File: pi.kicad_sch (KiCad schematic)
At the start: 12 parts, among them CN2 539160208

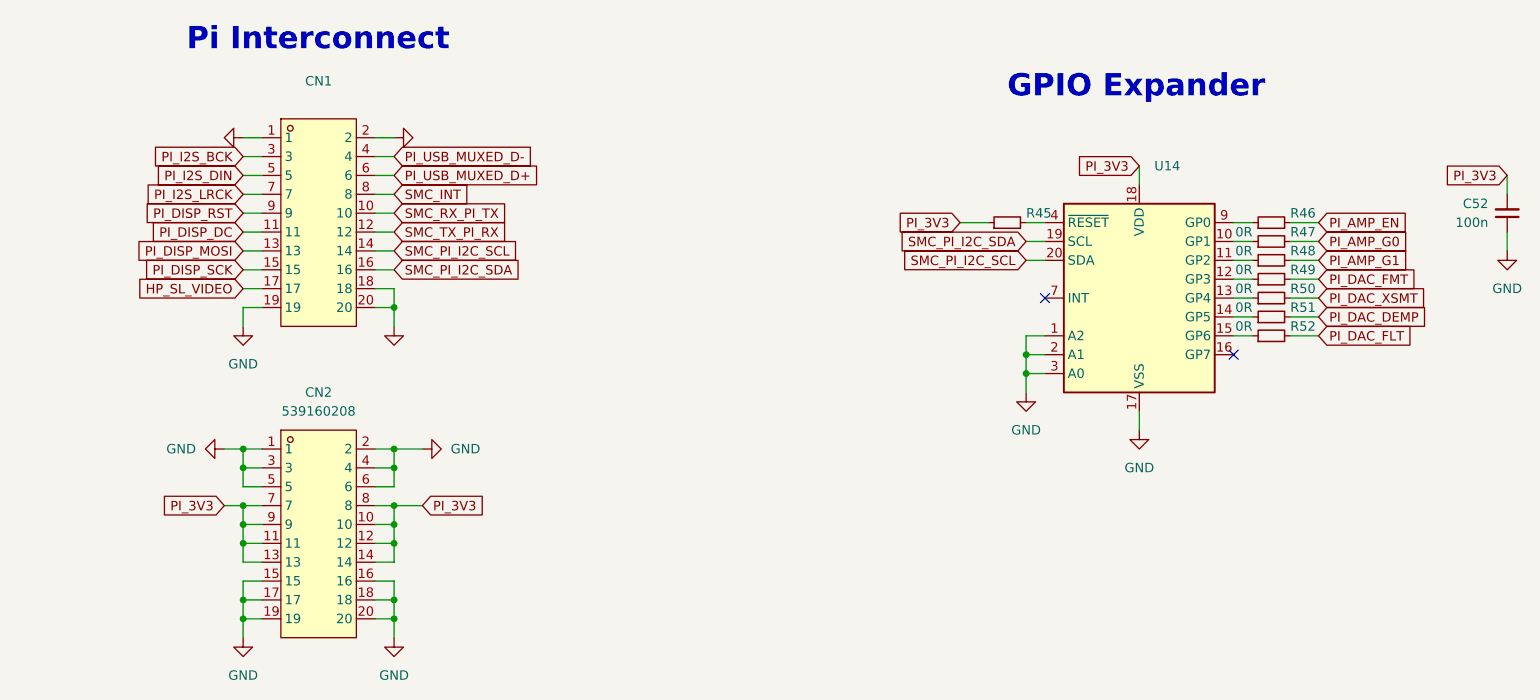
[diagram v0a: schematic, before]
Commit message: analysis: specify pi will be powered directly from VCC
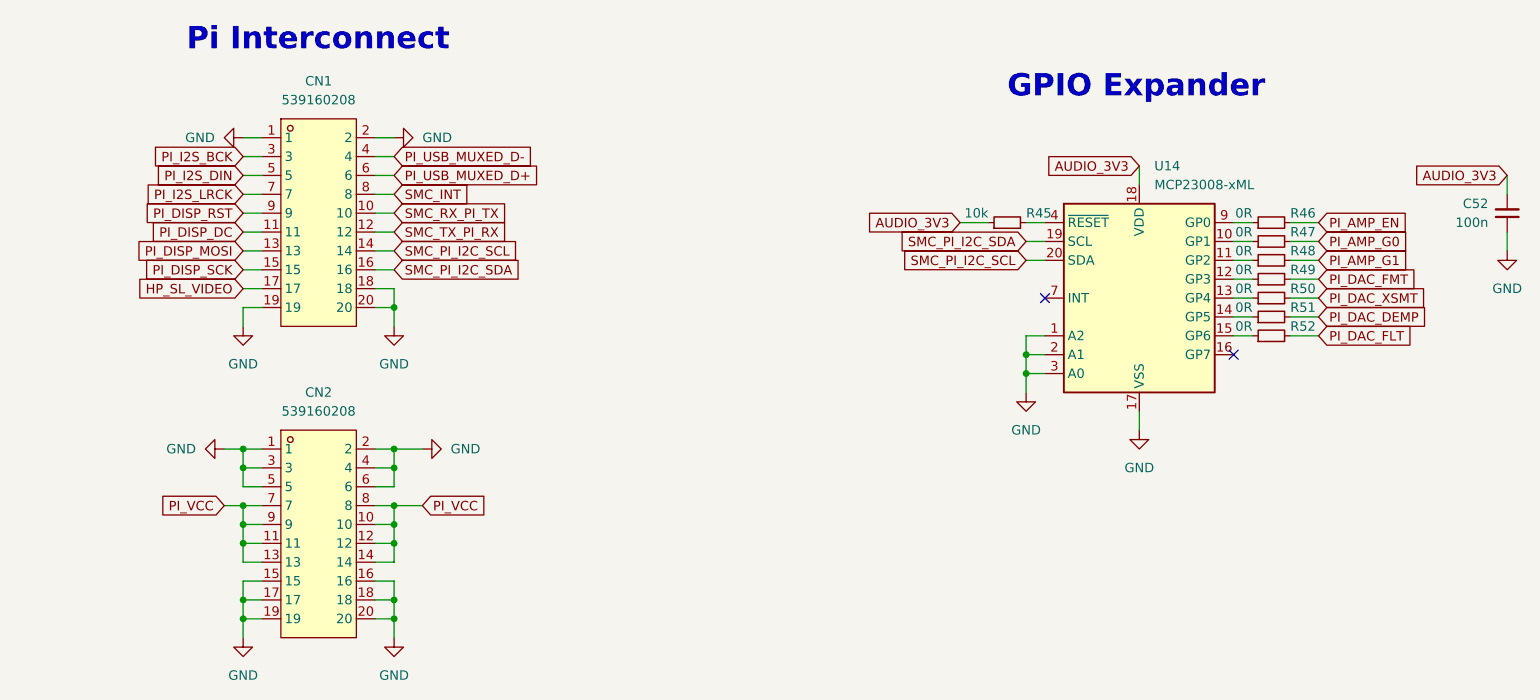
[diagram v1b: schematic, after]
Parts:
- C52: footprint (none) -> Capacitor_SMD:C_0402_1005Metric
- CN1: value (none) -> 539160208
- R45: value (none) -> 10k; footprint (none) -> Resistor_SMD:R_0402_1005Metric
- R46: value (none) -> 0R; footprint (none) -> Resistor_SMD:R_0402_1005Metric
- R47, R48, R49, R50, R51, R52: footprint (none) -> Resistor_SMD:R_0402_1005Metric
- U14: value (none) -> MCP23008-xML
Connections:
- net PI_3V3 renamed PI_VCC
- net PI_VCC: no longer C52.2, R45.1, U14.18 (VDD)
- new net AUDIO_3V3: C52.2, R45.1, U14.18 (VDD)
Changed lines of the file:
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@@
     (effects (font (size 3 3) (thickness 0.6) bold) (justify left bottom))
   )
+  (global_label "AUDIO_3V3" (shape input) (at 168.91 69.85 180) (fields_autoplaced)
+    (effects (font (size 1.27 1.27)) (justify right))
+    (property "Intersheet References" "${INTERSHEET_REFS}" (id 0) (at 156.3974 69.9294 0)
+      (effects (font (size 1.27 1.27)) (justify right) hide)
+    )
+  )
   (global_label "PI_AMP_G1" (shape input) (at 193.04 82.55 0) (fields_autoplaced)
     (effects (font (size 1.27 1.27)) (justify left))
@@
     )
   )
-  (global_label "PI_3V3" (shape input) (at 168.91 69.85 180) (fields_autoplaced)
-    (effects (font (size 1.27 1.27)) (justify right))
-    (property "Intersheet References" "${INTERSHEET_REFS}" (id 0) (at 160.1469 69.9294 0)
-      (effects (font (size 1.27 1.27)) (justify right) hide)
-    )
-  )
   (global_label "SMC_PI_I2C_SCL" (shape input) (at 153.67 82.55 180) (fields_autoplaced)
     (effects (font (size 1.27 1.27)) (justify right))
@@
     )
   )
-  (global_label "PI_3V3" (shape input) (at 144.78 77.47 180) (fields_autoplaced)
-    (effects (font (size 1.27 1.27)) (justify right))
-    (property "Intersheet References" "${INTERSHEET_REFS}" (id 0) (at 136.0169 77.5494 0)
-      (effects (font (size 1.27 1.27)) (justify right) hide)
-    )
-  )
   (global_label "PI_I2S_BCK" (shape input) (at 48.26 68.58 180) (fields_autoplaced)
     (effects (font (size 1.27 1.27)) (justify right))
@@
     )
   )
-  (global_label "PI_3V3" (shape input) (at 45.72 115.57 180) (fields_autoplaced)
+  (global_label "AUDIO_3V3" (shape input) (at 144.78 77.47 180) (fields_autoplaced)
+    (effects (font (size 1.27 1.27)) (justify right))
+    (property "Intersheet References" "${INTERSHEET_REFS}" (id 0) (at 132.2674 77.5494 0)
+      (effects (font (size 1.27 1.27)) (justify right) hide)
+    )
+  )
+  (global_label "PI_VCC" (shape input) (at 45.72 115.57 180) (fields_autoplaced)
     (effects (font (size 1.27 1.27)) (justify right))
     (property "Intersheet References" "${INTERSHEET_REFS}" (id 0) (at 36.9569 115.6494 0)
@@
     )
   )
-  (global_label "PI_3V3" (shape input) (at 72.39 115.57 0) (fields_autoplaced)
+  (global_label "PI_VCC" (shape input) (at 72.39 115.57 0) (fields_autoplaced)
     (effects (font (size 1.27 1.27)) (justify left))
     (property "Intersheet References" "${INTERSHEET_REFS}" (id 0) (at 81.1531 115.4906 0)
@@
     )
   )
-  (global_label "PI_3V3" (shape input) (at 218.44 71.12 180) (fields_autoplaced)
-    (effects (font (size 1.27 1.27)) (justify right))
-    (property "Intersheet References" "${INTERSHEET_REFS}" (id 0) (at 209.6769 71.1994 0)
+  (global_label "AUDIO_3V3" (shape input) (at 218.44 71.12 180) (fields_autoplaced)
+    (effects (font (size 1.27 1.27)) (justify right))
+    (property "Intersheet References" "${INTERSHEET_REFS}" (id 0) (at 205.9274 71.1994 0)
       (effects (font (size 1.27 1.27)) (justify right) hide)
     )
@@
       (effects (font (size 1.27 1.27)) (justify right))
     )
-    (property "Value" "" (id 1) (at 184.15 76.2 90)
-      (effects (font (size 1.27 1.27)) (justify left))
-    )
-    (property "Footprint" "" (id 2) (at 186.69 77.47 0)
+    (property "Value" "0R" (id 1) (at 184.15 76.2 90)
+      (effects (font (size 1.27 1.27)) (justify left))
+    )
+    (property "Footprint" "Resistor_SMD:R_0402_1005Metric" (id 2) (at 186.69 77.47 0)
       (effects (font (size 1.27 1.27)) hide)
     )
@@
       (effects (font (size 1.27 1.27)) (justify right))
     )
-    (property "Value" "" (id 1) (at 148.59 76.2 90)
-      (effects (font (size 1.27 1.27)) (justify left))
-    )
-    (property "Footprint" "" (id 2) (at 151.13 77.47 0)
+    (property "Value" "10k" (id 1) (at 148.59 76.2 90)
+      (effects (font (size 1.27 1.27)) (justify left))
+    )
+    (property "Footprint" "Resistor_SMD:R_0402_1005Metric" (id 2) (at 151.13 77.47 0)
       (effects (font (size 1.27 1.27)) hide)
     )
@@
       (effects (font (size 1.27 1.27)) (justify left))
     )
-    (property "Footprint" "" (id 2) (at 186.69 87.63 0)
+    (property "Footprint" "Resistor_SMD:R_0402_1005Metric" (id 2) (at 186.69 87.63 0)
       (effects (font (size 1.27 1.27)) hide)
     )
@@
       (effects (font (size 1.27 1.27)) (justify left))
     )
-    (property "Value" "" (id 1) (at 170.9294 72.39 0)
+    (property "Value" "MCP23008-xML" (id 1) (at 170.9294 72.39 0)
       (effects (font (size 1.27 1.27)) (justify left))
     )
@@
       (effects (font (size 1.27 1.27)) hide)
     )
-    (property "Value" "" (id 1) (at 68.58 96.52 0))
+    (property "Value" "GND" (id 1) (at 68.58 96.52 0))
     (property "Footprint" "" (id 2) (at 68.58 91.44 0)
       (effects (font (size 1.27 1.27)) hide)
@@
       (effects (font (size 1.27 1.27)) (justify left))
     )
-    (property "Footprint" "" (id 2) (at 186.69 92.71 0)
+    (property "Footprint" "Resistor_SMD:R_0402_1005Metric" (id 2) (at 186.69 92.71 0)
       (effects (font (size 1.27 1.27)) hide)
     )
@@
       (effects (font (size 1.27 1.27)) (justify left))
     )
-    (property "Footprint" "" (id 2) (at 186.69 85.09 0)
+    (property "Footprint" "Resistor_SMD:R_0402_1005Metric" (id 2) (at 186.69 85.09 0)
       (effects (font (size 1.27 1.27)) hide)
     )
@@
       (effects (font (size 1.27 1.27)) hide)
     )
-    (property "Value" "" (id 1) (at 72.39 66.0399 90)
+    (property "Value" "GND" (id 1) (at 72.39 66.0399 90)
       (effects (font (size 1.27 1.27)) (justify right))
     )
@@
       (effects (font (size 1.27 1.27)) (justify right))
     )
-    (property "Footprint" "" (id 2) (at 218.44 76.2 0)
+    (property "Footprint" "Capacitor_SMD:C_0402_1005Metric" (id 2) (at 218.44 76.2 0)
       (effects (font (size 1.27 1.27)) hide)
     )
@@
       (effects (font (size 1.27 1.27)) (justify left))
     )
-    (property "Footprint" "" (id 2) (at 186.69 90.17 0)
+    (property "Footprint" "Resistor_SMD:R_0402_1005Metric" (id 2) (at 186.69 90.17 0)
       (effects (font (size 1.27 1.27)) hide)
     )
@@
       (effects (font (size 1.27 1.27)) (justify left))
     )
-    (property "Footprint" "" (id 2) (at 186.69 80.01 0)
+    (property "Footprint" "Resistor_SMD:R_0402_1005Metric" (id 2) (at 186.69 80.01 0)
       (effects (font (size 1.27 1.27)) hide)
     )
@@
       (effects (font (size 1.27 1.27)) (justify left))
     )
-    (property "Footprint" "" (id 2) (at 186.69 82.55 0)
+    (property "Footprint" "Resistor_SMD:R_0402_1005Metric" (id 2) (at 186.69 82.55 0)
       (effects (font (size 1.27 1.27)) hide)
     )
@@
       (effects (font (size 1.27 1.27)) hide)
     )
-    (property "Value" "" (id 1) (at 44.45 66.0399 90)
+    (property "Value" "GND" (id 1) (at 44.45 66.0399 90)
       (effects (font (size 1.27 1.27)) (justify right))
     )
@@
     (in_bom yes) (on_board yes) (fields_autoplaced)
     (property "Reference" "CN1" (id 0) (at 58.42 58.42 0))
-    (property "Value" "" (id 1) (at 58.42 60.96 0))
+    (property "Value" "539160208" (id 1) (at 58.42 60.96 0))
     (property "Footprint" "lcsc:CONN-SMD_539160208" (id 2) (at 58.42 96.52 0)
       (effects (font (size 1.27 1.27)) hide)

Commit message: integration: add mounting holes and connectors and second board
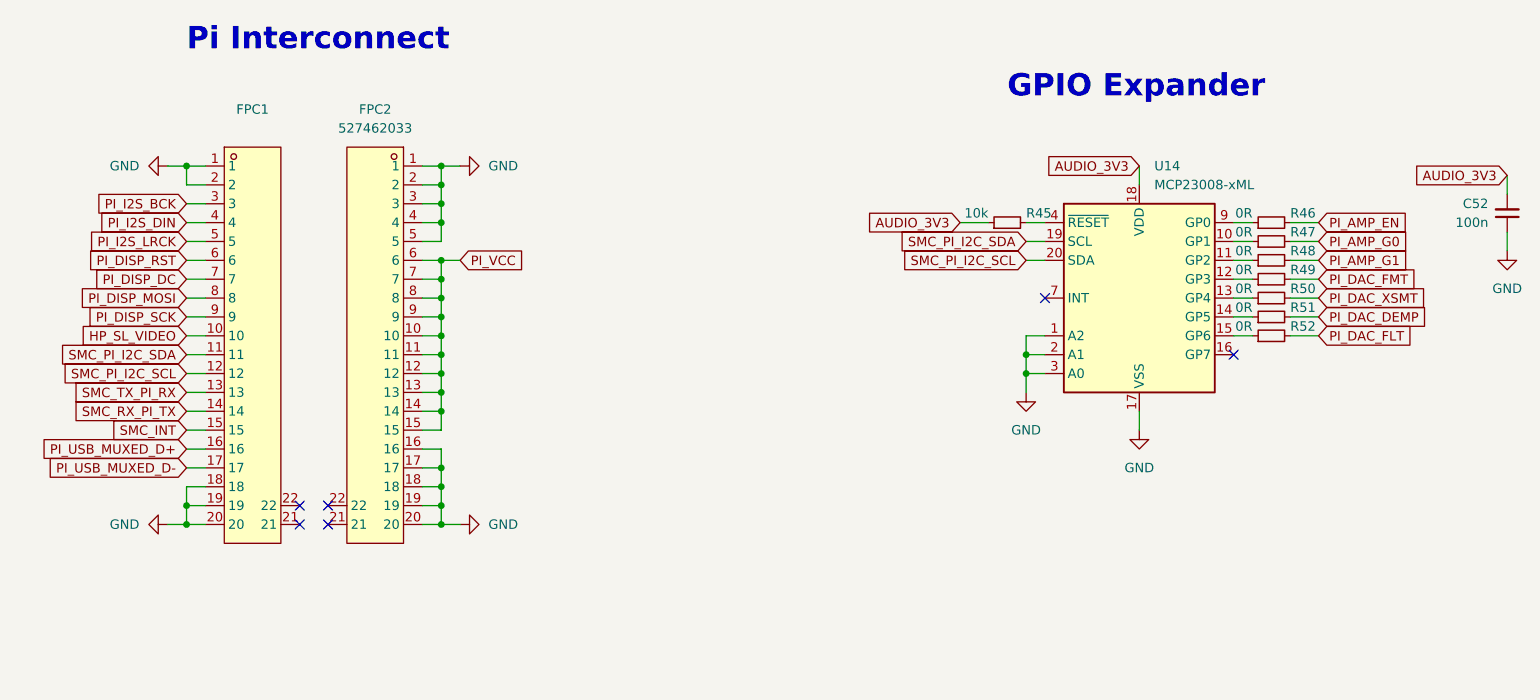
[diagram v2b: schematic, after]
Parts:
- removed CN1, CN2: 539160208, lcsc:CONN-SMD_539160208, symbol lcsc:539160208
- added FPC1: (no value), symbol lcsc:527462033
- added FPC2: 527462033, lcsc:FPC-SMD_527462033, symbol lcsc:527462033
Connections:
- net GND: now also FPC1.1, FPC1.18, FPC1.19, FPC1.2, FPC1.20, FPC2.1, FPC2.16, FPC2.17, FPC2.18, FPC2.19, FPC2.2, FPC2.20, FPC2.3, FPC2.4, FPC2.5
- net HP_SL_VIDEO: now also FPC1.10
- net PI_DISP_DC: now also FPC1.7
- net PI_DISP_MOSI: now also FPC1.8
- net PI_DISP_RST: now also FPC1.6
- net PI_DISP_SCK: now also FPC1.9
- net PI_I2S_BCK: now also FPC1.3
- net PI_I2S_DIN: now also FPC1.4
- net PI_I2S_LRCK: now also FPC1.5
- net PI_USB_MUXED_D+: now also FPC1.16
- net PI_USB_MUXED_D-: now also FPC1.17
- net PI_VCC: now also FPC2.10, FPC2.11, FPC2.12, FPC2.13, FPC2.14, FPC2.15, FPC2.6, FPC2.7, FPC2.8, FPC2.9
- net SMC_INT: now also FPC1.15
- net SMC_PI_I2C_SCL: now also FPC1.12
- net SMC_PI_I2C_SDA: now also FPC1.11
- net SMC_RX_PI_TX: now also FPC1.14
- net SMC_TX_PI_RX: now also FPC1.13
- no-connect marks 2 -> 6

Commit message: schem: migrate away from LCSC exclusive parts
- layout: migrate away from lcsc footprints
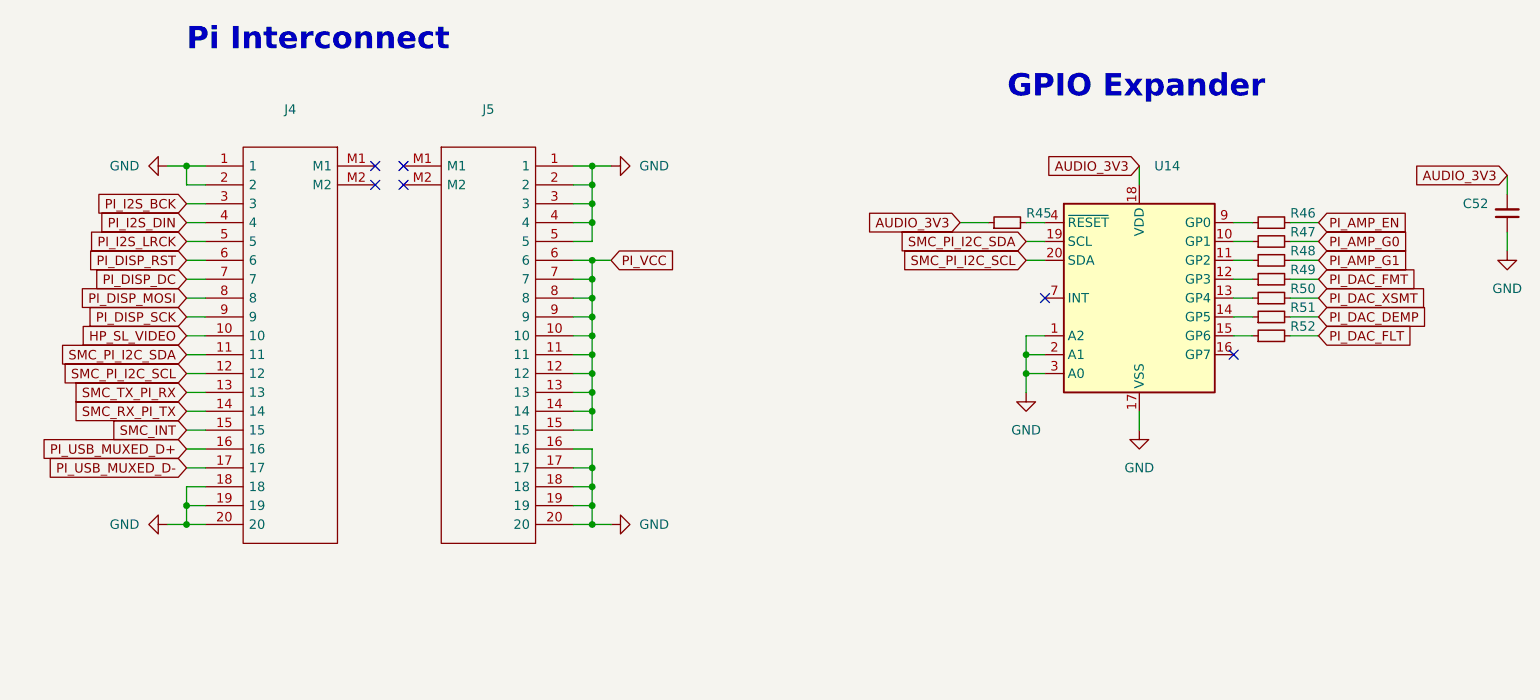
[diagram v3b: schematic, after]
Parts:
- removed FPC1: (no value), symbol lcsc:527462033
- removed FPC2: 527462033, lcsc:FPC-SMD_527462033, symbol lcsc:527462033
- added J4, J5: (no value), symbol gigahawk:2-1734839-0
- C52: value 100n -> (none); footprint Capacitor_SMD:C_0402_1005Metric -> (none)
- R45: value 10k -> (none); footprint Resistor_SMD:R_0402_1005Metric -> (none)
- R46, R47, R48, R49, R50, R51, R52: value 0R -> (none); footprint Resistor_SMD:R_0402_1005Metric -> (none)
- U14: value MCP23008-xML -> (none); footprint Package_DFN_QFN:QFN-20-1EP_4x4mm_P0.5mm_EP2.7x2.7mm -> (none); Digikey Part (none) -> MCP23008-E/ML-ND; Digikey Price/Stock (none) -> https://www.digikey.ca/en/products/detail/microchip-technol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; JLC Part (none) -> Extended Part; LCSC Part (none) -> C144211; Manufacturer (none) -> Microchip Technology; Manufacturer Part (none) -> MCP23008-E/ML; Mouser Part (none) -> 579-MCP23008-E/ML; Mouser Price/Stock (none) -> https://www.mouser.ca/ProductDetail/Microchip-Technology-At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
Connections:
- net GND: now also J4.1, J4.18, J4.19, J4.2, J4.20, J5.1, J5.16, J5.17, J5.18, J5.19, J5.2, J5.20, J5.3, J5.4, J5.5
- net HP_SL_VIDEO: now also J4.10
- net PI_DISP_DC: now also J4.7
- net PI_DISP_MOSI: now also J4.8
- net PI_DISP_RST: now also J4.6
- net PI_DISP_SCK: now also J4.9
- net PI_I2S_BCK: now also J4.3
- net PI_I2S_DIN: now also J4.4
- net PI_I2S_LRCK: now also J4.5
- net PI_USB_MUXED_D+: now also J4.16
- net PI_USB_MUXED_D-: now also J4.17
- net PI_VCC: now also J5.10, J5.11, J5.12, J5.13, J5.14, J5.15, J5.6, J5.7, J5.8, J5.9
- net SMC_INT: now also J4.15
- net SMC_PI_I2C_SCL: now also J4.12
- net SMC_PI_I2C_SDA: now also J4.11
- net SMC_RX_PI_TX: now also J4.14
- net SMC_TX_PI_RX: now also J4.13
